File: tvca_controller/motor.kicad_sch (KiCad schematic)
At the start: 3 parts, among them M1 Motor_DC, U3 BD6222HFP, U4 74LVC1G19

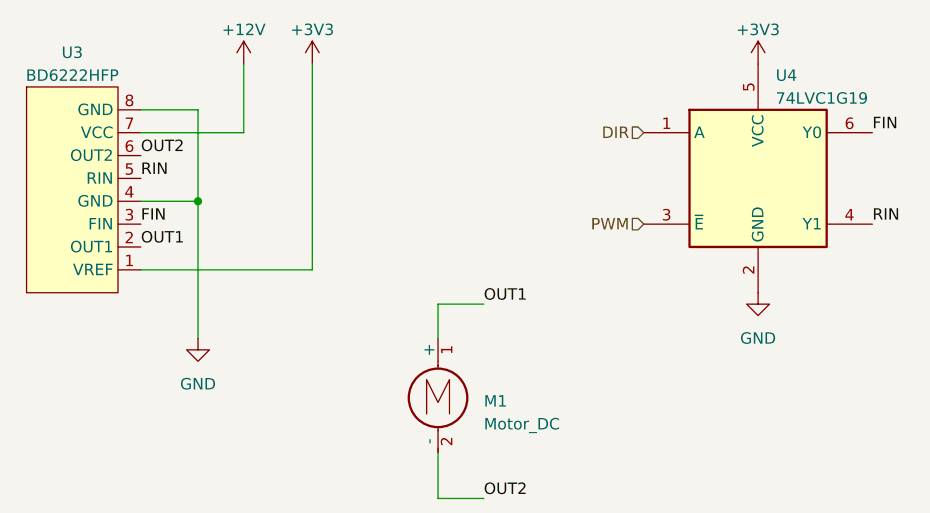
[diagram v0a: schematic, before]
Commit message: remove zips, refactor PCB to use software in place of 2-bit mux
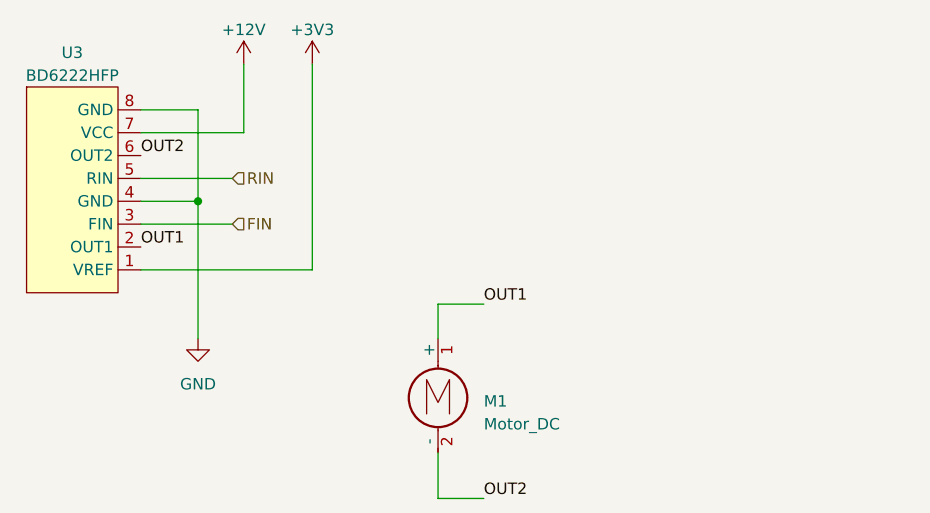
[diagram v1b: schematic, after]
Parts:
- removed U4: 74LVC1G19, symbol 74xGxx:74LVC1G19
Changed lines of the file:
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@@
+    (stroke (width 0) (type default))
+  )
+  (wire (pts (xy 118.11 88.9) (xy 107.95 88.9))
     (stroke (width 0) (type default))
   )
   (wire (pts (xy 146.05 124.46) (xy 140.97 124.46))
+    (stroke (width 0) (type default))
+  )
+  (wire (pts (xy 118.11 93.98) (xy 107.95 93.98))
     (stroke (width 0) (type default))
   )
@@
     (effects (font (size 1.27 1.27)) (justify left bottom))
   )
-  (label "FIN" (at 107.95 93.98 0) (fields_autoplaced)
-    (effects (font (size 1.27 1.27)) (justify left bottom))
-  )
   (label "OUT2" (at 146.05 124.46 0) (fields_autoplaced)
-    (effects (font (size 1.27 1.27)) (justify left bottom))
-  )
-  (label "RIN" (at 107.95 88.9 0) (fields_autoplaced)
-    (effects (font (size 1.27 1.27)) (justify left bottom))
-  )
-  (label "FIN" (at 189.23 83.82 0) (fields_autoplaced)
     (effects (font (size 1.27 1.27)) (justify left bottom))
   )
@@
     (effects (font (size 1.27 1.27)) (justify left bottom))
   )
-  (label "RIN" (at 189.23 93.98 0) (fields_autoplaced)
-    (effects (font (size 1.27 1.27)) (justify left bottom))
-  )
   (label "OUT1" (at 107.95 96.52 0) (fields_autoplaced)
     (effects (font (size 1.27 1.27)) (justify left bottom))
   )
-  (hierarchical_label "PWM" (shape input) (at 163.83 93.98 180) (fields_autoplaced)
-    (effects (font (size 1.27 1.27)) (justify right))
+  (hierarchical_label "FIN" (shape input) (at 118.11 93.98 0) (fields_autoplaced)
+    (effects (font (size 1.27 1.27)) (justify left))
   )
-  (hierarchical_label "DIR" (shape input) (at 163.83 83.82 180) (fields_autoplaced)
-    (effects (font (size 1.27 1.27)) (justify right))
-  )
-  (symbol (lib_id "power:GND") (at 176.53 101.6 0) (unit 1)
-    (in_bom yes) (on_board yes) (dnp no) (fields_autoplaced)
-    (property "Reference" "#PWR015" (at 176.53 107.95 0)
-      (effects (font (size 1.27 1.27)) hide)
-    )
-    (property "Value" "GND" (at 176.53 106.68 0)
-      (effects (font (size 1.27 1.27)))
-    )
-    (property "Footprint" "" (at 176.53 101.6 0)
-      (effects (font (size 1.27 1.27)) hide)
-    )
-    (property "Datasheet" "" (at 176.53 101.6 0)
-      (effects (font (size 1.27 1.27)) hide)
-    )
-    (pin "1")
-    (instances
-      (project "tvca_controller"
-        (path "/f08602f6-65d5-48ec-b5dd-079a575e1be0"
-          (reference "#PWR015") (unit 1)
-        )
-        (path "/f08602f6-65d5-48ec-b5dd-079a575e1be0/de8e002c-85d6-4a68-b910-e72b1e3d7295"
-          (reference "#PWR016") (unit 1)
-        )
-        (path "/f08602f6-65d5-48ec-b5dd-079a575e1be0/683c4c4a-2712-4619-b371-c4b4e0f76f26"
-          (reference "#PWR016") (unit 1)
-        )
-      )
-    )
+  (hierarchical_label "RIN" (shape input) (at 118.11 88.9 0) (fields_autoplaced)
+    (effects (font (size 1.27 1.27)) (justify left))
   )
   (symbol (lib_id "power:+3V3") (at 127 76.2 0) (unit 1)
@@
         )
       )
-    )
-  )
-  (symbol (lib_id "74xGxx:74LVC1G19") (at 176.53 88.9 0) (unit 1)
-    (in_bom yes) (on_board yes) (dnp no) (fields_autoplaced)
-    (property "Reference" "U4" (at 178.4859 77.47 0)
-      (effects (font (size 1.27 1.27)) (justify left))
-    )
-    (property "Value" "74LVC1G19" (at 178.4859 80.01 0)
-      (effects (font (size 1.27 1.27)) (justify left))
-    )
-    (property "Footprint" "" (at 176.53 88.9 0)
-      (effects (font (size 1.27 1.27)) hide)
-    )
-    (property "Datasheet" "http://www.ti.com/lit/sg/scyt129e/scyt129e.pdf" (at 176.53 88.9 0)
-      (effects (font (size 1.27 1.27)) hide)
-    )
-    (pin "1")
-    (pin "2")
-    (pin "3")
-    (pin "4")
-    (pin "5")
-    (pin "6")
-    (instances
-      (project "tvca_controller"
-        (path "/f08602f6-65d5-48ec-b5dd-079a575e1be0"
-          (reference "U4") (unit 1)
-        )
-        (path "/f08602f6-65d5-48ec-b5dd-079a575e1be0/de8e002c-85d6-4a68-b910-e72b1e3d7295"
-          (reference "U4") (unit 1)
-        )
-        (path "/f08602f6-65d5-48ec-b5dd-079a575e1be0/683c4c4a-2712-4619-b371-c4b4e0f76f26"
-          (reference "U4") (unit 1)
-        )
-      )
-    )
-  )
-  (symbol (lib_id "power:+3V3") (at 176.53 76.2 0) (unit 1)
-    (in_bom yes) (on_board yes) (dnp no)
-    (property "Reference" "#PWR016" (at 176.53 80.01 0)
-      (effects (font (size 1.27 1.27)) hide)
-    )
-    (property "Value" "+3V3" (at 176.53 72.39 0)
-      (effects (font (size 1.27 1.27)))
-    )
-    (property "Footprint" "" (at 176.53 76.2 0)
-      (effects (font (size 1.27 1.27)) hide)
-    )
-    (property "Datasheet" "" (at 176.53 76.2 0)
-      (effects (font (size 1.27 1.27)) hide)
-    )
-    (pin "1")
-    (instances
-      (project "tvca_controller"
-        (path "/f08602f6-65d5-48ec-b5dd-079a575e1be0"
-          (reference "#PWR016") (unit 1)
-        )
-        (path "/f08602f6-65d5-48ec-b5dd-079a575e1be0/de8e002c-85d6-4a68-b910-e72b1e3d7295"
-          (reference "#PWR015") (unit 1)
-        )
-        (path "/f08602f6-65d5-48ec-b5dd-079a575e1be0/683c4c4a-2712-4619-b371-c4b4e0f76f26"
-          (reference "#PWR015") (unit 1)
-        )
-      )

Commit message: add connectors
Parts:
- removed M1: Motor_DC, symbol Motor:Motor_DC
- added J3: Encoder Connection - ATM103-V, symbol Connector:Screw_Terminal_01x05
- added J5: Motor Connector, symbol Connector:Screw_Terminal_01x02
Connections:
- net GND: now also J3.5 (Pin_5)
- net OUT1: now also J5.1 (Pin_1)
- net OUT2: now also J5.2 (Pin_2)
- net +12V renamed POW
- new net +5V: J3.2 (Pin_2)
- new net A: J3.3 (Pin_3)
- new net B: J3.1 (Pin_1)
- no-connect marks 0 -> 1
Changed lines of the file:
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@@
   (junction (at 114.3 91.44) (diameter 0) (color 0 0 0 0)
   )
+  (no_connect (at 165.1 80.01))
+  (wire (pts (xy 160.02 72.39) (xy 165.1 72.39))
+    (stroke (width 0) (type default))
+  )
   (wire (pts (xy 127 99.06) (xy 127 76.2))
     (stroke (width 0) (type default))
@@
     (stroke (width 0) (type default))
   )
+  (wire (pts (xy 163.83 111.76) (xy 166.37 111.76))
+    (stroke (width 0) (type default))
+  )
   (wire (pts (xy 107.95 91.44) (xy 114.3 91.44))
     (stroke (width 0) (type default))
   )
-  (wire (pts (xy 146.05 102.87) (xy 140.97 102.87))
-    (stroke (width 0) (type default))
-  )
-  (wire (pts (xy 140.97 102.87) (xy 140.97 106.68))
+  (wire (pts (xy 162.56 63.5) (xy 162.56 74.93))
+    (stroke (width 0) (type default))
+  )
+  (wire (pts (xy 162.56 82.55) (xy 162.56 91.44))
+    (stroke (width 0) (type default))
+  )
+  (wire (pts (xy 160.02 77.47) (xy 165.1 77.47))
+    (stroke (width 0) (type default))
+  )
+  (wire (pts (xy 165.1 74.93) (xy 162.56 74.93))
     (stroke (width 0) (type default))
   )
@@
     (stroke (width 0) (type default))
   )
-  (wire (pts (xy 140.97 124.46) (xy 140.97 119.38))
-    (stroke (width 0) (type default))
-  )
   (wire (pts (xy 114.3 81.28) (xy 114.3 91.44))
     (stroke (width 0) (type default))
@@
     (stroke (width 0) (type default))
   )
-  (wire (pts (xy 146.05 124.46) (xy 140.97 124.46))
-    (stroke (width 0) (type default))
-  )
   (wire (pts (xy 118.11 93.98) (xy 107.95 93.98))
     (stroke (width 0) (type default))
@@
     (stroke (width 0) (type default))
   )
-  (label "OUT1" (at 146.05 102.87 0) (fields_autoplaced)
-    (effects (font (size 1.27 1.27)) (justify left bottom))
-  )
-  (label "OUT2" (at 146.05 124.46 0) (fields_autoplaced)
-    (effects (font (size 1.27 1.27)) (justify left bottom))
+  (wire (pts (xy 165.1 82.55) (xy 162.56 82.55))
+    (stroke (width 0) (type default))
+  )
+  (wire (pts (xy 163.83 109.22) (xy 166.37 109.22))
+    (stroke (width 0) (type default))
+  )
+  (label "OUT1" (at 163.83 109.22 180) (fields_autoplaced)
+    (effects (font (size 1.27 1.27)) (justify right bottom))
+  )
+  (label "OUT2" (at 163.83 111.76 180) (fields_autoplaced)
+    (effects (font (size 1.27 1.27)) (justify right bottom))
   )
   (label "OUT2" (at 107.95 86.36 0) (fields_autoplaced)
@@
     (effects (font (size 1.27 1.27)) (justify left bottom))
   )
+  (hierarchical_label "B" (shape input) (at 160.02 72.39 180) (fields_autoplaced)
+    (effects (font (size 1.27 1.27)) (justify right))
+  )
+  (hierarchical_label "A" (shape input) (at 160.02 77.47 180) (fields_autoplaced)
+    (effects (font (size 1.27 1.27)) (justify right))
+  )
   (hierarchical_label "FIN" (shape input) (at 118.11 93.98 0) (fields_autoplaced)
     (effects (font (size 1.27 1.27)) (justify left))
@@
   (hierarchical_label "RIN" (shape input) (at 118.11 88.9 0) (fields_autoplaced)
     (effects (font (size 1.27 1.27)) (justify left))
+  )
+  (hierarchical_label "POW" (shape input) (at 119.38 76.2 90) (fields_autoplaced)
+    (effects (font (size 1.27 1.27)) (justify left))
+  )
+  (symbol (lib_id "power:+5V") (at 162.56 63.5 0) (unit 1)
+    (in_bom yes) (on_board yes) (dnp no) (fields_autoplaced)
+    (property "Reference" "#PWR015" (at 162.56 67.31 0)
+      (effects (font (size 1.27 1.27)) hide)
+    )
+    (property "Value" "+5V" (at 162.56 59.69 0)
+      (effects (font (size 1.27 1.27)))
+    )
+    (property "Footprint" "" (at 162.56 63.5 0)
+      (effects (font (size 1.27 1.27)) hide)
+    )
+    (property "Datasheet" "" (at 162.56 63.5 0)
+      (effects (font (size 1.27 1.27)) hide)
+    )
+    (pin "1")
+    (instances
+      (project "tvca_controller"
+        (path "/f08602f6-65d5-48ec-b5dd-079a575e1be0/de8e002c-85d6-4a68-b910-e72b1e3d7295"
+          (reference "#PWR015") (unit 1)
+        )
+        (path "/f08602f6-65d5-48ec-b5dd-079a575e1be0/683c4c4a-2712-4619-b371-c4b4e0f76f26"
+          (reference "#PWR016") (unit 1)
+        )
+      )
+    )
   )
   (symbol (lib_id "power:+3V3") (at 127 76.2 0) (unit 1)
@@
     )
   )
-  (symbol (lib_id "power:+12V") (at 119.38 76.2 0) (unit 1)
-    (in_bom yes) (on_board yes) (dnp no)
-    (property "Reference" "#PWR013" (at 119.38 80.01 0)
-      (effects (font (size 1.27 1.27)) hide)
-    )
-    (property "Value" "+12V" (at 119.38 72.39 0)
-      (effects (font (size 1.27 1.27)))
-    )
-    (property "Footprint" "" (at 119.38 76.2 0)
-      (effects (font (size 1.27 1.27)) hide)
-    )
-    (property "Datasheet" "" (at 119.38 76.2 0)
-      (effects (font (size 1.27 1.27)) hide)
-    )
-    (pin "1")
-    (instances
-      (project "tvca_controller"
-        (path "/f08602f6-65d5-48ec-b5dd-079a575e1be0"
-          (reference "#PWR013") (unit 1)
-        )
-        (path "/f08602f6-65d5-48ec-b5dd-079a575e1be0/de8e002c-85d6-4a68-b910-e72b1e3d7295"
-          (reference "#PWR013") (unit 1)
-        )
-        (path "/f08602f6-65d5-48ec-b5dd-079a575e1be0/683c4c4a-2712-4619-b371-c4b4e0f76f26"
-          (reference "#PWR013") (unit 1)
+  (symbol (lib_id "power:GND") (at 162.56 91.44 0) (unit 1)
+    (in_bom yes) (on_board yes) (dnp no) (fields_autoplaced)
+    (property "Reference" "#PWR022" (at 162.56 97.79 0)
+      (effects (font (size 1.27 1.27)) hide)
+    )
+    (property "Value" "GND" (at 162.56 96.52 0)
+      (effects (font (size 1.27 1.27)))
+    )
+    (property "Footprint" "" (at 162.56 91.44 0)
+      (effects (font (size 1.27 1.27)) hide)
+    )
+    (property "Datasheet" "" (at 162.56 91.44 0)
+      (effects (font (size 1.27 1.27)) hide)
+    )
+    (pin "1")
+    (instances
+      (project "tvca_controller"
+        (path "/f08602f6-65d5-48ec-b5dd-079a575e1be0/de8e002c-85d6-4a68-b910-e72b1e3d7295"
+          (reference "#PWR022") (unit 1)
+        )
+        (path "/f08602f6-65d5-48ec-b5dd-079a575e1be0/683c4c4a-2712-4619-b371-c4b4e0f76f26"
+          (reference "#PWR023") (unit 1)
+        )
+      )
+    )
+  )
+  (symbol (lib_id "Connector:Screw_Terminal_01x05") (at 170.18 77.47 0) (unit 1)
+    (in_bom yes) (on_board yes) (dnp no) (fields_autoplaced)
+    (property "Reference" "J3" (at 172.72 76.835 0)
+      (effects (font (size 1.27 1.27)) (justify left))
+    )
+    (property "Value" "Encoder Connection - ATM103-V" (at 172.72 79.375 0)
+      (effects (font (size 1.27 1.27)) (justify left))
+    )
+    (property "Footprint" "" (at 170.18 77.47 0)
+      (effects (font (size 1.27 1.27)) hide)
+    )
+    (property "Datasheet" "~" (at 170.18 77.47 0)
+      (effects (font (size 1.27 1.27)) hide)
+    )
+    (pin "1")
+    (pin "2")
+    (pin "3")
+    (pin "4")
+    (pin "5")
+    (instances
+      (project "tvca_controller"
+        (path "/f08602f6-65d5-48ec-b5dd-079a575e1be0/de8e002c-85d6-4a68-b910-e72b1e3d7295"
+          (reference "J3") (unit 1)
+        )
+        (path "/f08602f6-65d5-48ec-b5dd-079a575e1be0/683c4c4a-2712-4619-b371-c4b4e0f76f26"
+          (reference "J4") (unit 1)
+        )
+      )
+    )
+  )
+  (symbol (lib_id "Connector:Screw_Terminal_01x02") (at 171.45 109.22 0) (unit 1)
+    (in_bom yes) (on_board yes) (dnp no) (fields_autoplaced)
+    (property "Reference" "J5" (at 173.99 109.855 0)
+      (effects (font (size 1.27 1.27)) (justify left))
+    )
+    (property "Value" "Motor Connector" (at 173.99 112.395 0)
+      (effects (font (size 1.27 1.27)) (justify left))
+    )
+    (property "Footprint" "" (at 171.45 109.22 0)
+      (effects (font (size 1.27 1.27)) hide)
+    )
+    (property "Datasheet" "~" (at 171.45 109.22 0)
+      (effects (font (size 1.27 1.27)) hide)
+    )
+    (pin "1")
+    (pin "2")
+    (instances
+      (project "tvca_controller"
+        (path "/f08602f6-65d5-48ec-b5dd-079a575e1be0/de8e002c-85d6-4a68-b910-e72b1e3d7295"
+          (reference "J5") (unit 1)
+        )
+        (path "/f08602f6-65d5-48ec-b5dd-079a575e1be0/683c4c4a-2712-4619-b371-c4b4e0f76f26"
+          (reference "J6") (unit 1)
         )
       )
@@
         )
       )
-    )
-  )
-  (symbol (lib_id "Motor:Motor_DC") (at 140.97 111.76 0) (unit 1)
-    (in_bom yes) (on_board yes) (dnp no) (fields_autoplaced)
-    (property "Reference" "M1" (at 146.05 113.665 0)
-      (effects (font (size 1.27 1.27)) (justify left))
-    )
-    (property "Value" "Motor_DC" (at 146.05 116.205 0)
-      (effects (font (size 1.27 1.27)) (justify left))
-    )
-    (property "Footprint" "" (at 140.97 114.046 0)
-      (effects (font (size 1.27 1.27)) hide)
-    )
-    (property "Datasheet" "~" (at 140.97 114.046 0)
-      (effects (font (size 1.27 1.27)) hide)
-    )
-    (pin "1")
-    (pin "2")
-    (instances
-      (project "tvca_controller"
-        (path "/f08602f6-65d5-48ec-b5dd-079a575e1be0"
-          (reference "M1") (unit 1)
-        )
-        (path "/f08602f6-65d5-48ec-b5dd-079a575e1be0/de8e002c-85d6-4a68-b910-e72b1e3d7295"
-          (reference "M1") (unit 1)
-        )
-        (path "/f08602f6-65d5-48ec-b5dd-079a575e1be0/683c4c4a-2712-4619-b371-c4b4e0f76f26"
-          (reference "M1") (unit 1)
-        )
-      )
